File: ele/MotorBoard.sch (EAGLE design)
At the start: 19 parts

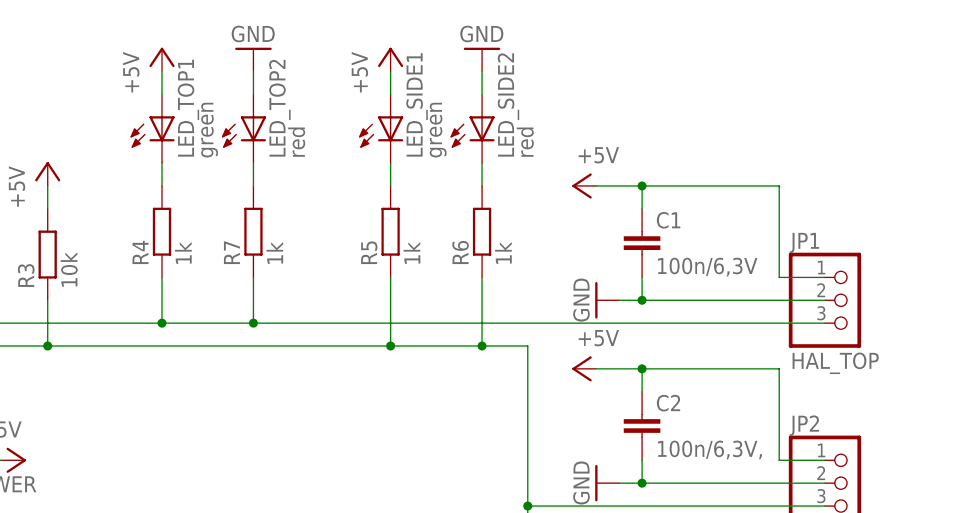
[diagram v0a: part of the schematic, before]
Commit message: ele: MotorBoard - fix the bug with the LEDs
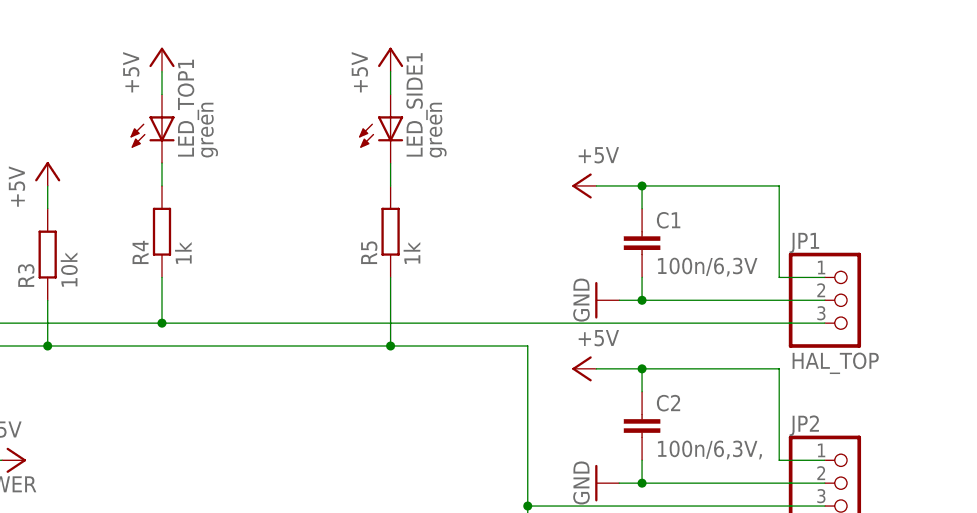
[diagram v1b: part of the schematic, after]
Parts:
- removed LED_SIDE2, LED_TOP2: red, led:LEDCHIPLED_0603
- removed R6, R7: 1k, rcl:R-EU_R0603
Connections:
- removed net LED_SIDE2: LED_SIDE2.C, R6.2
- removed net LED_TOP2: LED_TOP2.C, R7.2
- net GND: no longer LED_SIDE2.A, LED_TOP2.A
- net HAL_SIDE: no longer R6.1
- net HAL_TOP: no longer R7.1
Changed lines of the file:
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@@
 </part>
 <part name="P+8" library="supply1" library_urn="urn:adsk.eagle:library:371" deviceset="+5V" device=""/>
-<part name="R6" library="rcl" library_urn="urn:adsk.eagle:library:334" deviceset="R-EU_" device="R0603" package3d_urn="urn:adsk.eagle:package:23555/2" value="1k"/>
-<part name="LED_SIDE2" library="led" deviceset="LED" device="CHIPLED_0603" value="red">
-<attribute name="DIGIKEY" value="160-1446-1-ND"/>
-<attribute name="FARNELL" value="2293494"/>
-<attribute name="MOUSER" value="859-LTST-C191KGKT"/>
-<attribute name="RS" value="872-1799"/>
-</part>
-<part name="R7" library="rcl" library_urn="urn:adsk.eagle:library:334" deviceset="R-EU_" device="R0603" package3d_urn="urn:adsk.eagle:package:23555/2" value="1k"/>
-<part name="LED_TOP2" library="led" deviceset="LED" device="CHIPLED_0603" value="red">
-<attribute name="DIGIKEY" value="160-1446-1-ND"/>
-<attribute name="FARNELL" value="2293494"/>
-<attribute name="MOUSER" value="859-LTST-C191KGKT"/>
-<attribute name="RS" value="872-1799"/>
-</part>
-<part name="GND4" library="supply1" deviceset="GND" device=""/>
-<part name="GND5" library="supply1" deviceset="GND" device=""/>
 <part name="C1" library="rcl" library_urn="urn:adsk.eagle:library:334" deviceset="C-EU" device="C0603" package3d_urn="urn:adsk.eagle:package:23616/2" value="100n/6,3V"/>
 <part name="C2" library="rcl" library_urn="urn:adsk.eagle:library:334" deviceset="C-EU" device="C0603" package3d_urn="urn:adsk.eagle:package:23616/2" value="100n/6,3V,"/>
@@
 </instance>
 <instance part="P+8" gate="1" x="96.52" y="93.98"/>
-<instance part="R6" gate="G$1" x="106.68" y="73.66" rot="R90"/>
-<instance part="LED_SIDE2" gate="G$1" x="106.68" y="86.36">
-<attribute name="DIGIKEY" x="106.68" y="86.36" size="1.778" layer="96" display="off"/>
-<attribute name="FARNELL" x="106.68" y="86.36" size="1.778" layer="96" display="off"/>
-<attribute name="MOUSER" x="106.68" y="86.36" size="1.778" layer="96" display="off"/>
-<attribute name="RS" x="106.68" y="86.36" size="1.778" layer="96" display="off"/>
-</instance>
-<instance part="R7" gate="G$1" x="81.28" y="73.66" rot="R90"/>
-<instance part="LED_TOP2" gate="G$1" x="81.28" y="86.36">
-<attribute name="DIGIKEY" x="81.28" y="86.36" size="1.778" layer="96" display="off"/>
-<attribute name="FARNELL" x="81.28" y="86.36" size="1.778" layer="96" display="off"/>
-<attribute name="MOUSER" x="81.28" y="86.36" size="1.778" layer="96" display="off"/>
-<attribute name="RS" x="81.28" y="86.36" size="1.778" layer="96" display="off"/>
-</instance>
-<instance part="GND4" gate="1" x="81.28" y="93.98" rot="MR180"/>
-<instance part="GND5" gate="1" x="106.68" y="93.98" rot="MR180"/>
 <instance part="C1" gate="G$1" x="124.46" y="73.66"/>
 <instance part="C2" gate="G$1" x="124.46" y="53.34"/>
@@
 </segment>
 <segment>
-<pinref part="LED_TOP2" gate="G$1" pin="A"/>
-<wire x1="81.28" y1="91.44" x2="81.28" y2="88.9" width="0.1524" layer="91"/>
-<pinref part="GND4" gate="1" pin="GND"/>
-</segment>
-<segment>
-<pinref part="LED_SIDE2" gate="G$1" pin="A"/>
-<wire x1="106.68" y1="91.44" x2="106.68" y2="88.9" width="0.1524" layer="91"/>
-<pinref part="GND5" gate="1" pin="GND"/>
-</segment>
-<segment>
 <pinref part="GND6" gate="1" pin="GND"/>
 <pinref part="JP4" gate="A" pin="2"/>
@@
 <pinref part="R4" gate="G$1" pin="1"/>
 <pinref part="JP1" gate="A" pin="3"/>
-<wire x1="144.78" y1="63.5" x2="81.28" y2="63.5" width="0.1524" layer="91"/>
+<wire x1="144.78" y1="63.5" x2="71.12" y2="63.5" width="0.1524" layer="91"/>
 <pinref part="JP3" gate="A" pin="2"/>
 <pinref part="R2" gate="G$1" pin="1"/>
-<wire x1="81.28" y1="63.5" x2="71.12" y2="63.5" width="0.1524" layer="91"/>
 <wire x1="71.12" y1="63.5" x2="48.26" y2="63.5" width="0.1524" layer="91"/>
 <wire x1="48.26" y1="63.5" x2="17.78" y2="63.5" width="0.1524" layer="91"/>
@@
 <wire x1="71.12" y1="68.58" x2="71.12" y2="63.5" width="0.1524" layer="91"/>
 <junction x="71.12" y="63.5"/>
-<pinref part="R7" gate="G$1" pin="1"/>
-<wire x1="81.28" y1="68.58" x2="81.28" y2="63.5" width="0.1524" layer="91"/>
-<junction x="81.28" y="63.5"/>
 <label x="25.4" y="63.5" size="1.778" layer="95"/>
 </segment>
@@
 <wire x1="96.52" y1="81.28" x2="96.52" y2="78.74" width="0.1524" layer="91"/>
 <pinref part="R5" gate="G$1" pin="2"/>
-</segment>
-</net>
-<net name="LED_SIDE2" class="0">
-<segment>
-<pinref part="LED_SIDE2" gate="G$1" pin="C"/>
-<wire x1="106.68" y1="81.28" x2="106.68" y2="78.74" width="0.1524" layer="91"/>
-<pinref part="R6" gate="G$1" pin="2"/>
-</segment>
-</net>
-<net name="LED_TOP2" class="0">
-<segment>
-<pinref part="LED_TOP2" gate="G$1" pin="C"/>
-<wire x1="81.28" y1="81.28" x2="81.28" y2="78.74" width="0.1524" layer="91"/>
-<pinref part="R7" gate="G$1" pin="2"/>
 </segment>
 </net>
@@
 <wire x1="17.78" y1="60.96" x2="58.42" y2="60.96" width="0.1524" layer="91"/>
 <wire x1="58.42" y1="60.96" x2="96.52" y2="60.96" width="0.1524" layer="91"/>
-<wire x1="96.52" y1="60.96" x2="106.68" y2="60.96" width="0.1524" layer="91"/>
-<wire x1="106.68" y1="60.96" x2="111.76" y2="60.96" width="0.1524" layer="91"/>
+<wire x1="96.52" y1="60.96" x2="111.76" y2="60.96" width="0.1524" layer="91"/>
 <wire x1="111.76" y1="60.96" x2="111.76" y2="43.18" width="0.1524" layer="91"/>
 <pinref part="JP2" gate="A" pin="3"/>
@@
 <wire x1="96.52" y1="68.58" x2="96.52" y2="60.96" width="0.1524" layer="91"/>
 <junction x="96.52" y="60.96"/>
-<pinref part="R6" gate="G$1" pin="1"/>
-<wire x1="106.68" y1="68.58" x2="106.68" y2="60.96" width="0.1524" layer="91"/>
-<junction x="106.68" y="60.96"/>
 <label x="25.4" y="60.96" size="1.778" layer="95"/>
 <wire x1="111.76" y1="17.78" x2="111.76" y2="43.18" width="0.1524" layer="91"/>

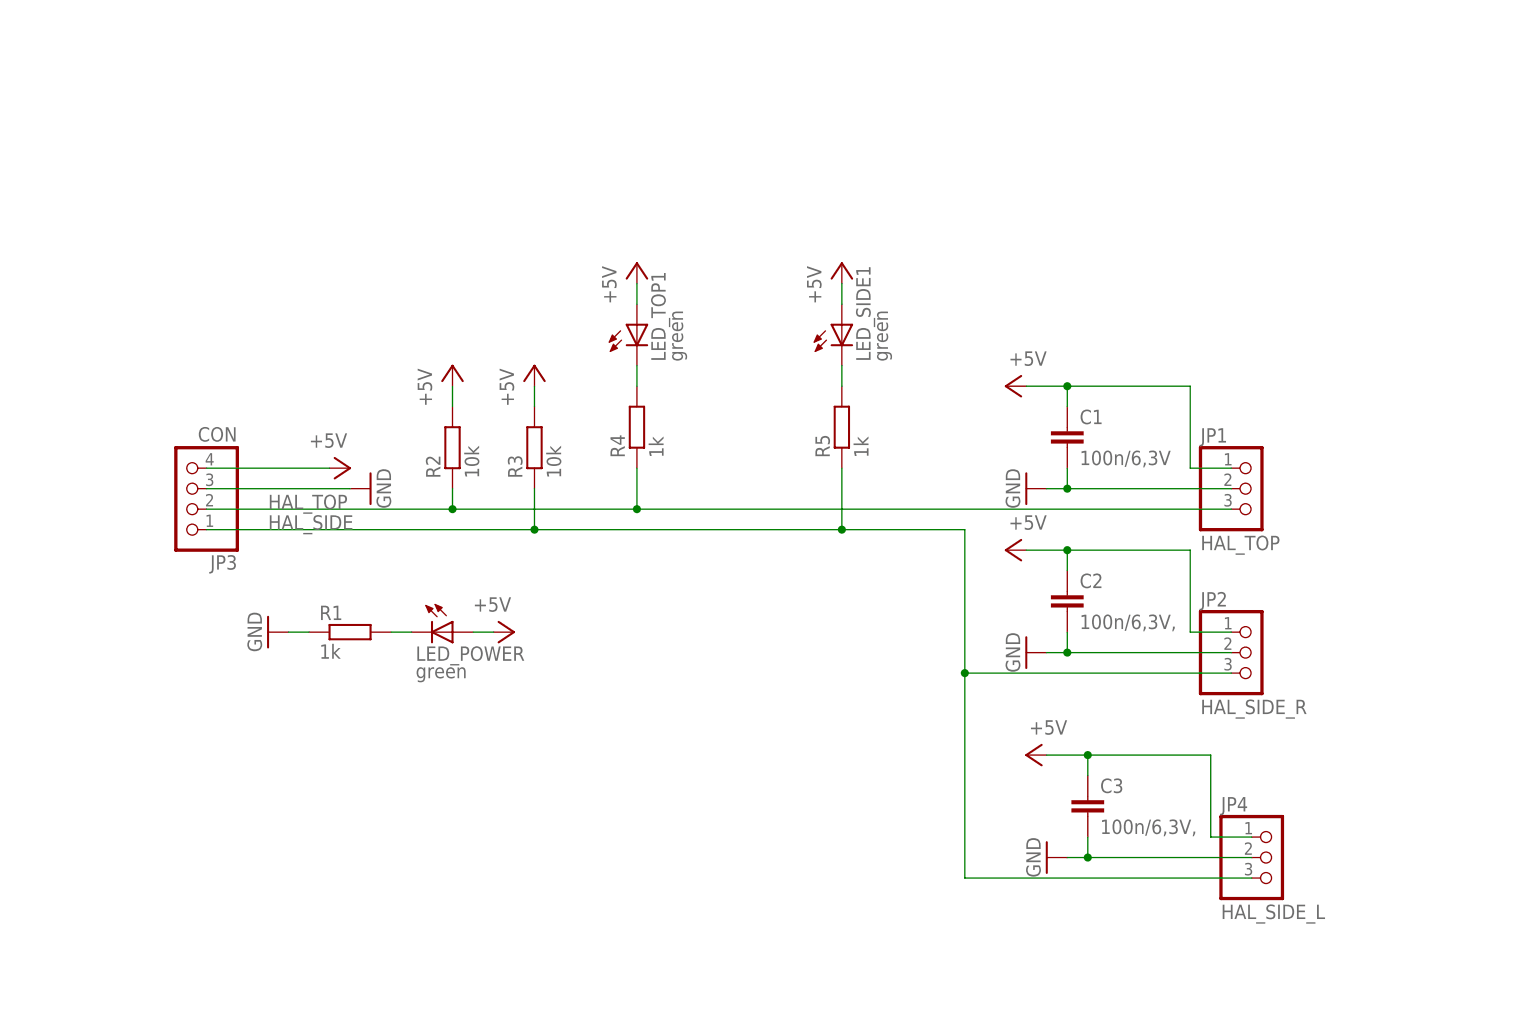
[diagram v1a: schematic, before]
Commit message: Add licenses to Eagle files
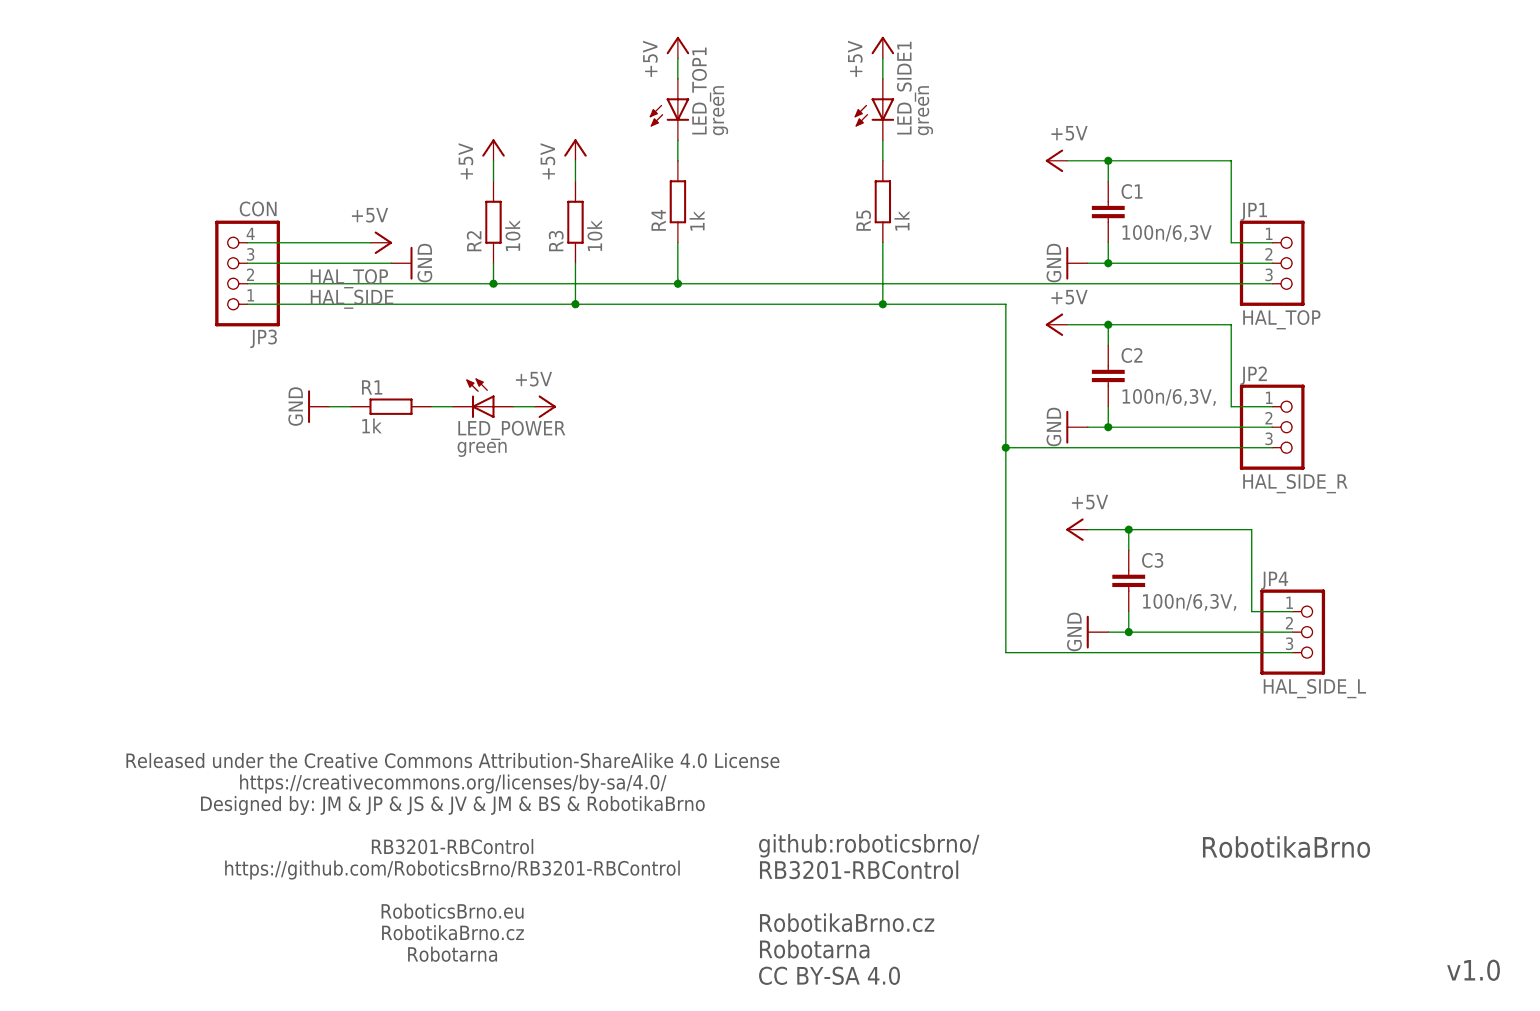
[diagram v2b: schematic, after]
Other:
- note added: "Released under the Creative Commons Attribution-ShareAlike 4.0 License https://creativecommons.org/licenses/by-sa/4.0/ Designed by: JM & JP & JS & JV & JM & BS & RobotikaBrno RB3201-RBControl https://github.com/RoboticsBrno/RB3201-RBControl RoboticsBrno.eu RobotikaBrno.cz Robotarna"
- note added: "RobotikaBrno"
- note added: "github:roboticsbrno/ RB3201-RBControl RobotikaBrno.cz Robotarna CC BY-SA 4.0"
- note added: "v1.0"
- moved on the sheet: C1, C2, C3, JP1, JP2, JP3, JP4, LED_POWER, LED_SIDE1, LED_TOP1, R1, R2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
